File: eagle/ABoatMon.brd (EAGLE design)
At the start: 57.5 x 36.2 mm, 20 parts

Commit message: Another go...
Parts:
- removed 5V: 5V, SparkFun-Connectors:1X02
- removed GND, GND_II: GND, SparkFun-Connectors:1X02
- added J1: 5V, SparkFun-Connectors:1X01
- added J2, J3: GND, SparkFun-Connectors:1X01
- moved C2 2.54 mm to (49.5, 10.2)
- moved R5 1.27 mm to (45.7, 12.7)
- moved VCC 0.13 mm to (2.54, 13.5)
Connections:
- net 3.3V: no longer MOTEINO_MEGA.3V3_2
- net 5V: now also J1.1; no longer 5V.1, 5V.2
- net GND: now also J2.1, J3.1; no longer GND.1, GND.2, GND_II.1, GND_II.2, MOTEINO_MEGA.GND_2
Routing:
- net VIN: track 87.7 -> 0.00 mm, vias 1 -> 0
- net 3.3V: track 86.9 -> 0.00 mm, vias 3 -> 0
- net N$1: track 72.9 -> 0.00 mm, vias 3 -> 0
- net D19_PWRON: track 63.2 -> 0.00 mm
- net D9_FONA_RX: track 59.3 -> 0.00 mm, vias 1 -> 0
- net D28_DS_DATA: track 56.7 -> 0.00 mm
- net D27_DS_PWR: track 55.6 -> 0.00 mm
- net D8_FONA_TX: track 53.2 -> 0.00 mm, vias 1 -> 0
- net VCC: track 47.9 -> 0.00 mm, vias 2 -> 0
- net D11_GPS_TX: track 45.7 -> 0.00 mm
- net D10_GPS_RX: track 43.4 -> 0.00 mm
- net D13_FONA_NETSTAT: track 39.9 -> 0.00 mm
- net D14_FONA_KEY: track 34.4 -> 0.00 mm
- net D25_LED_SWITCH: track 31.3 -> 0.00 mm
- net D3_BILGESW: track 30.0 -> 0.00 mm
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
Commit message: v 2.99
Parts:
- moved C2 12.0 mm to (43.2, 20.3)
- moved R2 10.2 mm to (17.8, 12.7)
- moved R6 10.2 mm to (31.8, 16.5), turned to 180 degrees
- moved R5 9.16 mm to (40.6, 20.3)
- moved R3 8.89 mm to (26.7, 9.02), turned to 0 degrees
- moved C1 7.83 mm to (29.1, 12.6), turned to 180 degrees
- moved R1 1.02 mm to (15.2, 2.79), turned to 18.7 degrees
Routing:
- net VIN: track 0.00 -> 101.8 mm, vias 0 -> 1
- net N$1: track 0.00 -> 83.2 mm, vias 0 -> 2
- net D8_FONA_TX: track 0.00 -> 51.7 mm, vias 0 -> 3
- net D9_FONA_RX: track 0.00 -> 51.1 mm, vias 0 -> 2
- net D27_DS_PWR: track 0.00 -> 48.3 mm, vias 0 -> 1
- net D28_DS_DATA: track 0.00 -> 46.5 mm, vias 0 -> 1
- net D19_PWRON: track 0.00 -> 45.9 mm, vias 0 -> 2
- net D3_BILGESW: track 0.00 -> 42.8 mm
- net D13_FONA_NETSTAT: track 0.00 -> 42.0 mm, vias 0 -> 2
- net D10_GPS_RX: track 0.00 -> 37.7 mm, vias 0 -> 1
- net D11_GPS_TX: track 0.00 -> 36.9 mm, vias 0 -> 1
- net D12_GPS_MOS_N: track 0.00 -> 34.8 mm
- net D26_LED: track 0.00 -> 34.4 mm, vias 0 -> 3
- net D14_FONA_KEY: track 0.00 -> 33.6 mm
- net D25_LED_SWITCH: track 0.00 -> 32.4 mm, vias 0 -> 1
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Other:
- board text added: "gregcope@gmail.com v2.99 AboatMon Shield"
- board text removed: "gregcope@gmail.com v1.99 AboatMon Shield"

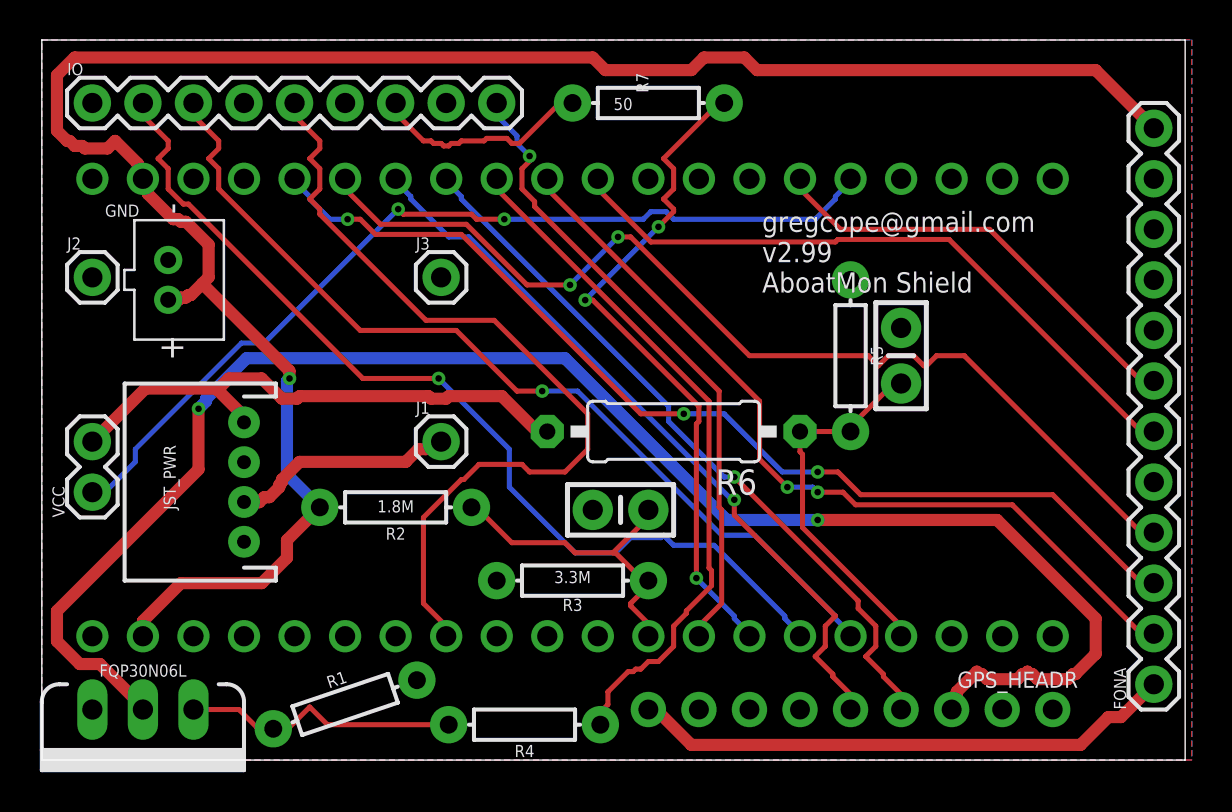
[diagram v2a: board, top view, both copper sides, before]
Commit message: simplified to use GPS enable pin, reduce BOM.  Need to remove 10K pull-up on Enable pin
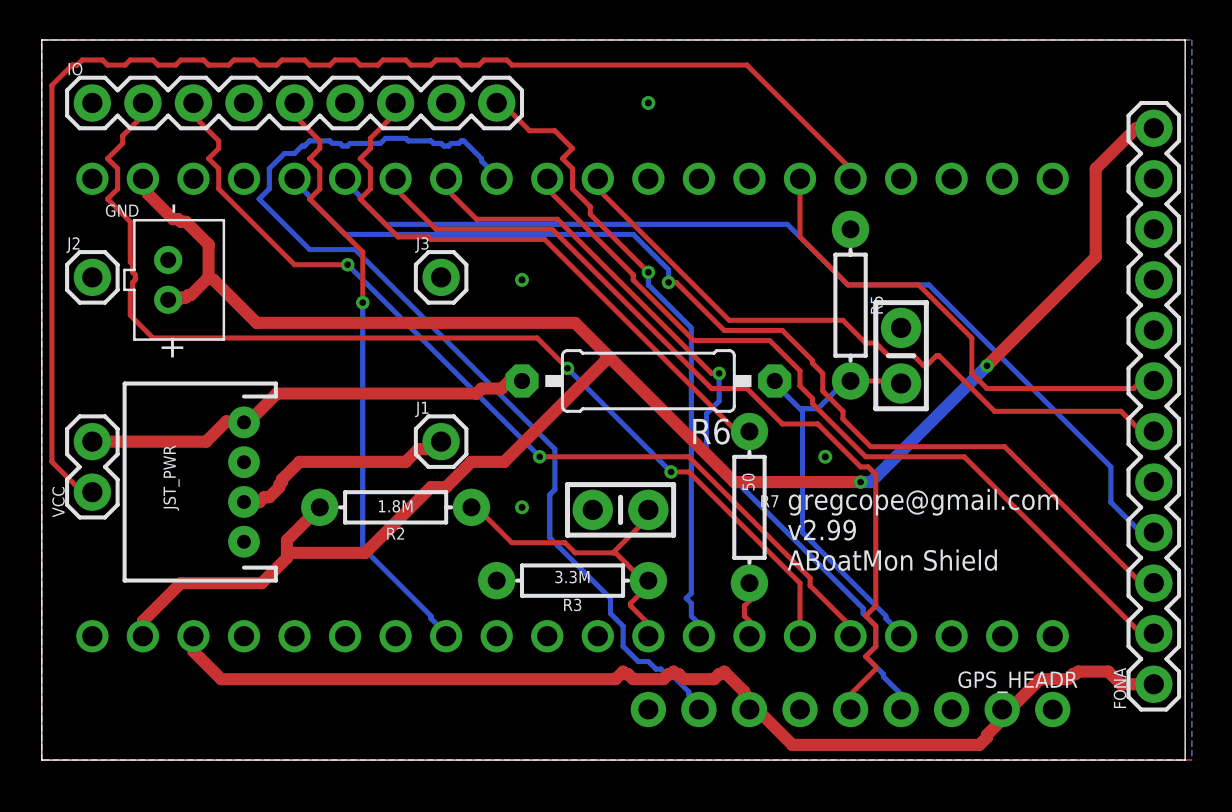
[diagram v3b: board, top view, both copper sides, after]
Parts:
- removed FQP30N06L: 60V/32A/35mΩ, SparkFun-DiscreteSemi:TO220V
- removed R1: 150, SparkFun-Resistors:AXIAL-0.3
- removed R4: 10k, SparkFun-Resistors:AXIAL-0.3
- moved R7 20.9 mm to (35.6, 12.7), turned to 270 degrees
- moved R6 2.84 mm to (30.5, 19.1)
- moved R5 2.54 mm to (40.6, 22.9)
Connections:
- removed net D12_GPS_MOS_N: MOTEINO_MEGA.D12, R4.P$1
- removed net N$1: FQP30N06L.2, JP1.3
- removed net N$3: FQP30N06L.1, R1.P$1, R4.P$2
- new net D12_GPS_ENABLE: JP1.8, MOTEINO_MEGA.D12
- net 3.3V: now also JP1.2, JP1.7, MOTEINO_MEGA.3V3; no longer JP1.9
- net GND: now also JP1.3; no longer FQP30N06L.3, R1.P$2
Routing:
- net N$1: track 83.2 -> 0.00 mm, vias 2 -> 0
- net D12_GPS_ENABLE: track 0.00 -> 52.2 mm
- net D12_GPS_MOS_N: track 34.8 -> 0.00 mm
- net D26_LED: track 34.4 -> 2.88 mm, vias 3 -> 0
- net 3.3V: track 27.4 -> 54.5 mm
- net D19_PWRON: track 45.9 -> 66.7 mm, vias 2 -> 0
- net N$2: track 11.2 -> 30.4 mm
- net N$3: track 14.1 -> 0.00 mm
- net D3_BILGESW: track 42.8 -> 30.8 mm, vias 0 -> 1
- net D10_GPS_RX: track 37.7 -> 43.8 mm, vias 1 -> 0
- net D27_DS_PWR: track 48.3 -> 54.4 mm, vias 1 -> 2
- net VCC: track 27.7 -> 22.9 mm
- net D11_GPS_TX: track 36.9 -> 39.7 mm
- net D18_FONA_PS: track 22.3 -> 25.1 mm
- net A5_VCC_VD: track 18.7 -> 21.1 mm
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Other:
- board text added: "gregcope@gmail.com v2.99 ABoatMon Shield"
- board text removed: "gregcope@gmail.com v2.99 AboatMon Shield"

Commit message: doco added
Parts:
- moved R3 8.89 mm to (17.8, 9.02)
- moved R6 5.08 mm to (30.5, 24.1)
- moved R7 3.81 mm to (35.6, 16.5)
- moved FONA 2.84 mm to (54.6, 6.35)
- moved C1 2.54 mm to (26.5, 12.6)
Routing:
- net VIN: track 103.7 -> 0.00 mm, vias 2 -> 0
- net D19_PWRON: track 66.7 -> 0.00 mm
- net 3.3V: track 54.5 -> 0.00 mm
- net D27_DS_PWR: track 54.4 -> 0.00 mm, vias 2 -> 0
- net D8_FONA_TX: track 52.9 -> 0.00 mm, vias 1 -> 0
- net D12_GPS_ENABLE: track 52.2 -> 0.00 mm
- net D9_FONA_RX: track 49.2 -> 0.00 mm
- net D28_DS_DATA: track 46.8 -> 0.00 mm, vias 2 -> 0
- net D10_GPS_RX: track 43.8 -> 0.00 mm
- net D13_FONA_NETSTAT: track 41.0 -> 0.00 mm
- net D11_GPS_TX: track 39.7 -> 0.00 mm, vias 1 -> 0
- net D14_FONA_KEY: track 33.9 -> 0.00 mm
- net D25_LED_SWITCH: track 32.5 -> 0.00 mm, vias 1 -> 0
- net D3_BILGESW: track 30.8 -> 0.00 mm, vias 1 -> 0
- net N$2: track 30.4 -> 0.00 mm
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
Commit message: rollback
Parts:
- moved R3 8.89 mm to (26.7, 9.02)
- moved R6 5.08 mm to (30.5, 19.1)
- moved R7 3.81 mm to (35.6, 12.7)
- moved FONA 2.84 mm to (55.9, 3.81)
- moved C1 2.54 mm to (29.1, 12.6)
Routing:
- net VIN: track 0.00 -> 103.7 mm, vias 0 -> 2
- net D19_PWRON: track 0.00 -> 66.7 mm
- net 3.3V: track 0.00 -> 54.5 mm
- net D27_DS_PWR: track 0.00 -> 54.4 mm, vias 0 -> 2
- net D8_FONA_TX: track 0.00 -> 52.9 mm, vias 0 -> 1
- net D12_GPS_ENABLE: track 0.00 -> 52.2 mm
- net D9_FONA_RX: track 0.00 -> 49.2 mm
- net D28_DS_DATA: track 0.00 -> 46.8 mm, vias 0 -> 2
- net D10_GPS_RX: track 0.00 -> 43.8 mm
- net D13_FONA_NETSTAT: track 0.00 -> 41.0 mm
- net D11_GPS_TX: track 0.00 -> 39.7 mm, vias 0 -> 1
- net D14_FONA_KEY: track 0.00 -> 33.9 mm
- net D25_LED_SWITCH: track 0.00 -> 32.5 mm, vias 0 -> 1
- net D3_BILGESW: track 0.00 -> 30.8 mm, vias 0 -> 1
- net N$2: track 0.00 -> 30.4 mm
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
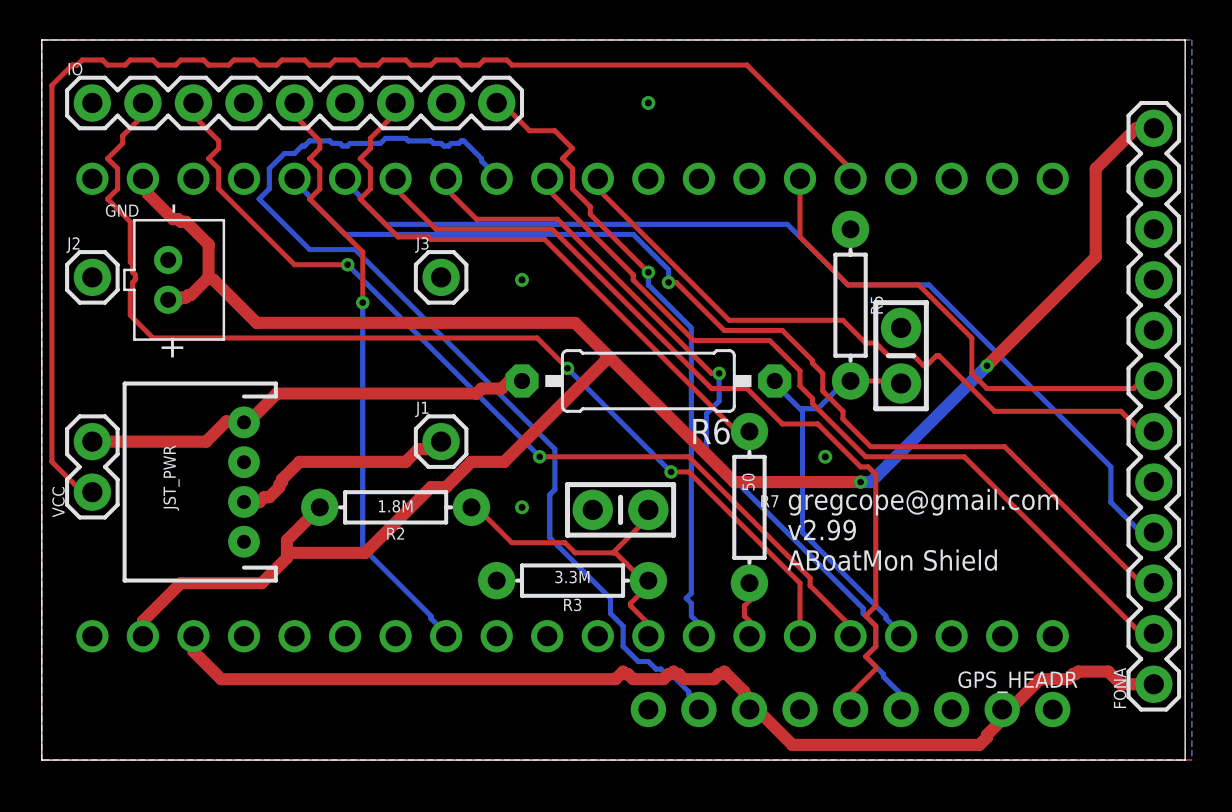
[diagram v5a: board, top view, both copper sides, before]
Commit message: Smaller layout, swapped gps
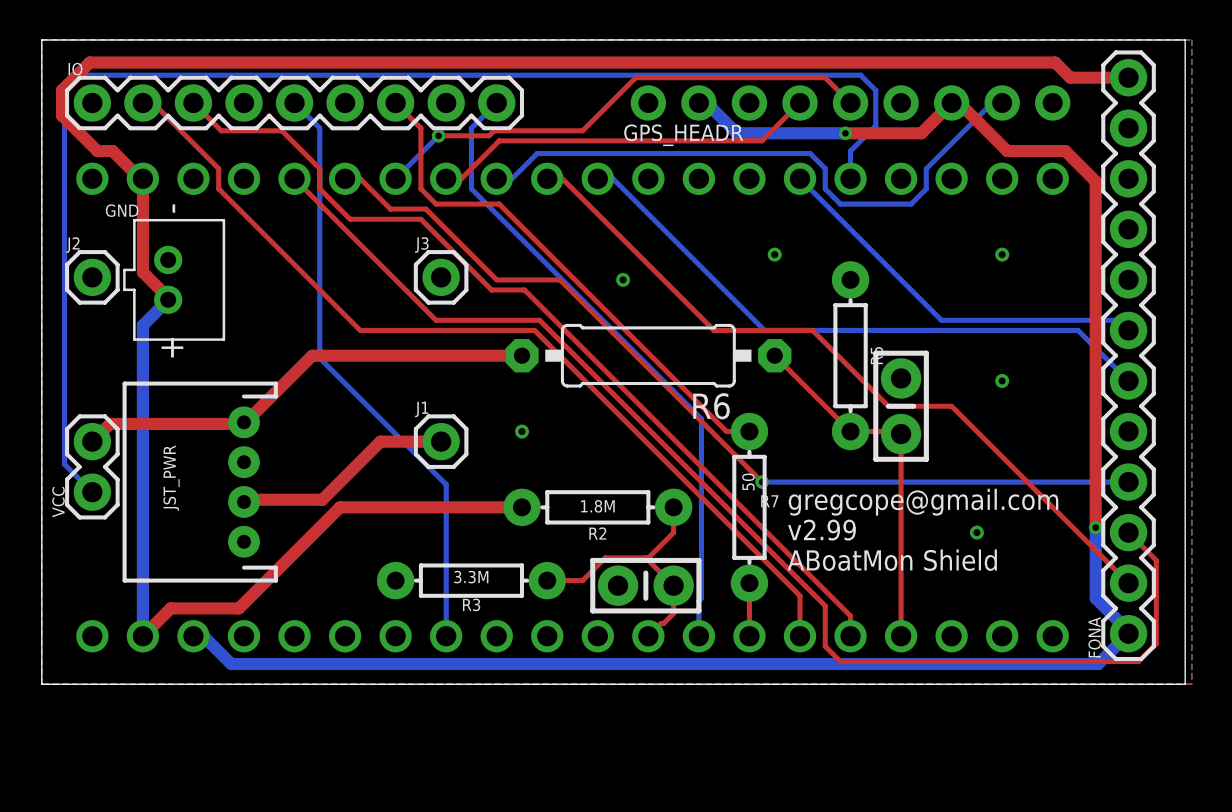
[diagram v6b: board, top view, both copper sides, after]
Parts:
- moved JP1 30.5 mm to (40.6, 33.0), turned to 0 degrees
- moved R2 10.2 mm to (27.9, 12.7)
- moved R3 5.08 mm to (21.6, 9.02)
- moved C1 4.02 mm to (30.4, 8.76)
- moved FONA 2.84 mm to (54.6, 6.35)
- moved C2 2.54 mm to (43.2, 17.8)
- moved R5 2.54 mm to (40.6, 20.3)
- moved R6 1.27 mm to (30.5, 20.3)
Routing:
- net 3.3V: track 54.5 -> 94.4 mm, vias 0 -> 2
- net D12_GPS_ENABLE: track 52.2 -> 30.3 mm
- net D11_GPS_TX: track 39.7 -> 19.4 mm, vias 1 -> 0
- net D10_GPS_RX: track 43.8 -> 25.5 mm, vias 0 -> 1
- net D27_DS_PWR: track 54.4 -> 45.9 mm, vias 2 -> 0
- net D8_FONA_TX: track 52.9 -> 61.1 mm, vias 1 -> 0
- net D18_FONA_PS: track 25.1 -> 19.7 mm
- net N$2: track 30.4 -> 26.4 mm
- net D9_FONA_RX: track 49.2 -> 45.7 mm, vias 0 -> 1
- net A0: track 17.2 -> 13.7 mm
- net D13_FONA_NETSTAT: track 41.0 -> 37.6 mm
- net VIN: track 103.7 -> 106.9 mm, vias 2 -> 0
- net D14_FONA_KEY: track 33.9 -> 30.9 mm
- net A5_VCC_VD: track 21.1 -> 18.1 mm
- net D28_DS_DATA: track 46.8 -> 45.3 mm, vias 2 -> 0
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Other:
- board size 57.5 x 36.2 mm -> 57.5 x 32.4 mm

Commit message: Silkscreen updates
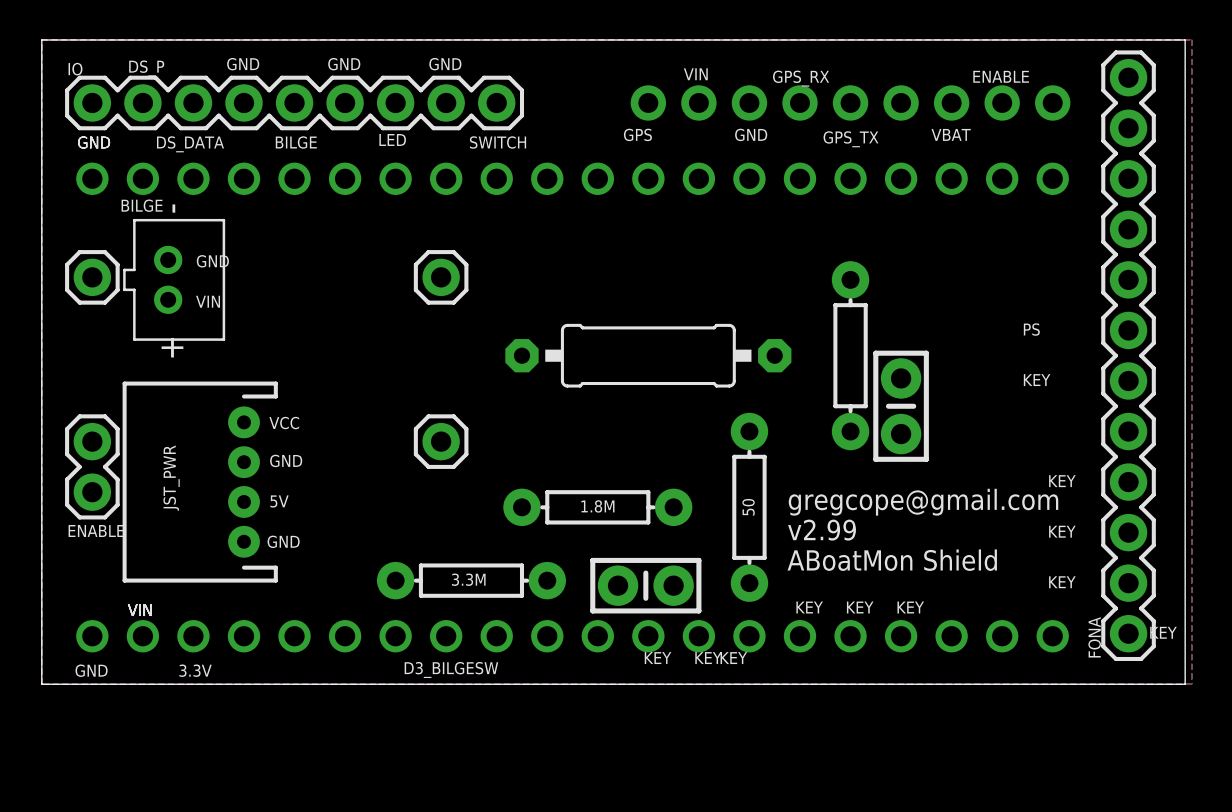
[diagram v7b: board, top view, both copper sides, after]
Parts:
- JP1: value GPS_HEADR -> GPS
- turned C1 to 0 degrees
- renumbered VCC to ENABLE
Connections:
- net N$2 renamed LED
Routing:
- net VIN: track 106.9 -> 0.00 mm
- net 3.3V: track 94.4 -> 0.00 mm, vias 2 -> 0
- net D19_PWRON: track 67.1 -> 0.00 mm
- net D8_FONA_TX: track 61.1 -> 0.00 mm
- net D27_DS_PWR: track 45.9 -> 0.00 mm
- net D9_FONA_RX: track 45.7 -> 0.00 mm, vias 1 -> 0
- net D28_DS_DATA: track 45.3 -> 0.00 mm
- net D13_FONA_NETSTAT: track 37.6 -> 0.00 mm
- net D25_LED_SWITCH: track 32.2 -> 0.00 mm
- net D14_FONA_KEY: track 30.9 -> 0.00 mm
- net D12_GPS_ENABLE: track 30.3 -> 0.00 mm
- net D3_BILGESW: track 30.0 -> 0.00 mm
- net LED: track 26.4 -> 0.00 mm
- net D10_GPS_RX: track 25.5 -> 0.00 mm, vias 1 -> 0
- net VCC: track 23.4 -> 0.00 mm
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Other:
- board text added: "3.3V"
- board text added: "5V"
- board text added: "BILGE"
- board text added: "D3_BILGESW"
- board text added: "DS_DATA"
- board text added: "DS_P"
- board text added: "ENABLE"
- board text added: "GPS_RX"
- board text added: "GPS_TX"
- board text added: "KEY"
- board text added: "LED"
- board text added: "PS"
- board text added: "SWITCH"
- board text added: "VBAT"
- board text added: "VCC"
- board text added: "VIN"

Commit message: Silkscreen updates+routing
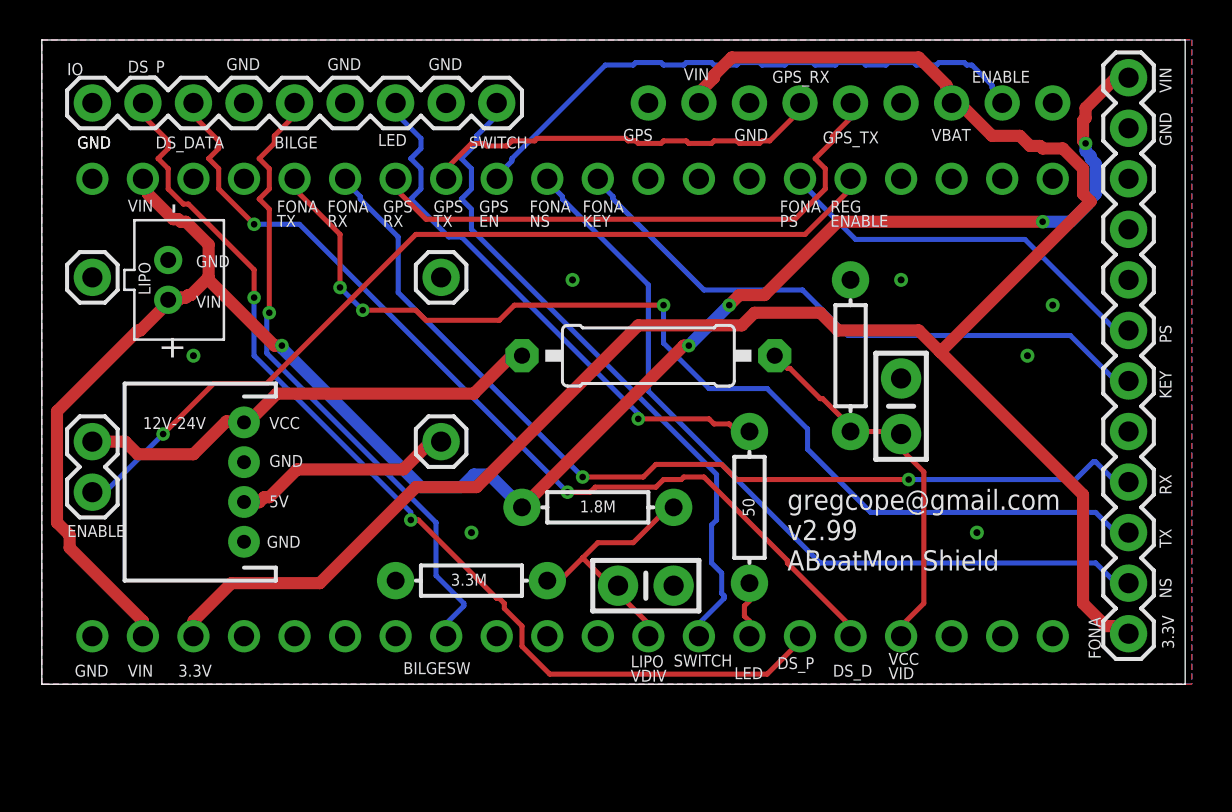
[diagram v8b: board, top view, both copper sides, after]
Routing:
- net 3.3V: track 0.00 -> 99.8 mm
- net VIN: track 0.00 -> 94.3 mm, vias 0 -> 5
- net D8_FONA_TX: track 0.00 -> 53.5 mm, vias 0 -> 3
- net D27_DS_PWR: track 0.00 -> 51.5 mm, vias 0 -> 2
- net D9_FONA_RX: track 0.00 -> 48.7 mm, vias 0 -> 2
- net D28_DS_DATA: track 0.00 -> 47.3 mm, vias 0 -> 2
- net D19_PWRON: track 0.00 -> 44.9 mm, vias 0 -> 1
- net D13_FONA_NETSTAT: track 0.00 -> 40.9 mm
- net D25_LED_SWITCH: track 0.00 -> 34.2 mm
- net D3_BILGESW: track 0.00 -> 32.7 mm, vias 0 -> 1
- net D14_FONA_KEY: track 0.00 -> 31.0 mm
- net D12_GPS_ENABLE: track 0.00 -> 29.7 mm
- net D10_GPS_RX: track 0.00 -> 28.6 mm
- net LED: track 0.00 -> 28.0 mm, vias 0 -> 1
- net VCC: track 0.00 -> 24.0 mm
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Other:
- board text added: "12V-24V"
- board text added: "BILGESW"
- board text added: "DS_D"
- board text added: "FONA KEY"
- board text added: "FONA NS"
- board text added: "FONA PS"
- board text added: "FONA RX"
- board text added: "FONA TX"
- board text added: "GPS EN"
- board text added: "GPS RX"
- board text added: "GPS TX"
- board text added: "LIPO"
- board text added: "LIPO VDIV"
- board text added: "NS"
- board text added: "REG ENABLE"
- board text added: "RX"
- board text added: "TX"
- board text added: "VCC VID"
- board text removed: "D3_BILGESW"
